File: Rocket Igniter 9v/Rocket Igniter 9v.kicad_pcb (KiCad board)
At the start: 2 copper layers, 79.9 x 59.8 mm, 29 parts, among them J1 1711725, J2 1711725, K1 G5Q-1 DC5, Q1 BC327, Q2 PN2222ABU, SW1 Y201132C203NQ, SW2 M2011S3S1W01, SW3 RP3502ARED

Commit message: tidied the pcb
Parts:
- D2: value 1.5KExxCA -> P6KE6.8CA; footprint Diode_THT:D_DO-201AE_P15.24mm_Horizontal -> Diode_THT:D_DO-15_P10.16mm_Horizontal
- moved R5 11.3 mm to (186.3, 65.6)
- moved SW1 5.90 mm to (195.1, 70.5), turned to 180 degrees
- moved SW3 5.38 mm to (187.0, 59.7), turned to 90 degrees
- moved LED3 4.10 mm to (179.9, 72.7)
- moved J2 1.33 mm to (221.0, 78.9)
- moved D2 1.11 mm to (170.4, 66.4)
- moved J1 0.48 mm to (157.0, 84.0)
- renumbered REF** to locked
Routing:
- net -BATT: track 14.8 -> 207.3 mm
- net Net-(D2-Pad1): track 36.9 -> 29.3 mm
- net Net-(LED3-Pad2): track 13.5 -> 6.13 mm
- net +5V: track 71.2 -> 77.2 mm
- net Net-(R5-Pad1): track 11.4 -> 6.45 mm
- net Net-(D2-Pad2): track 54.3 -> 51.8 mm
- removed copper zone on B.Cu, net -BATT
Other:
- net class Default removed

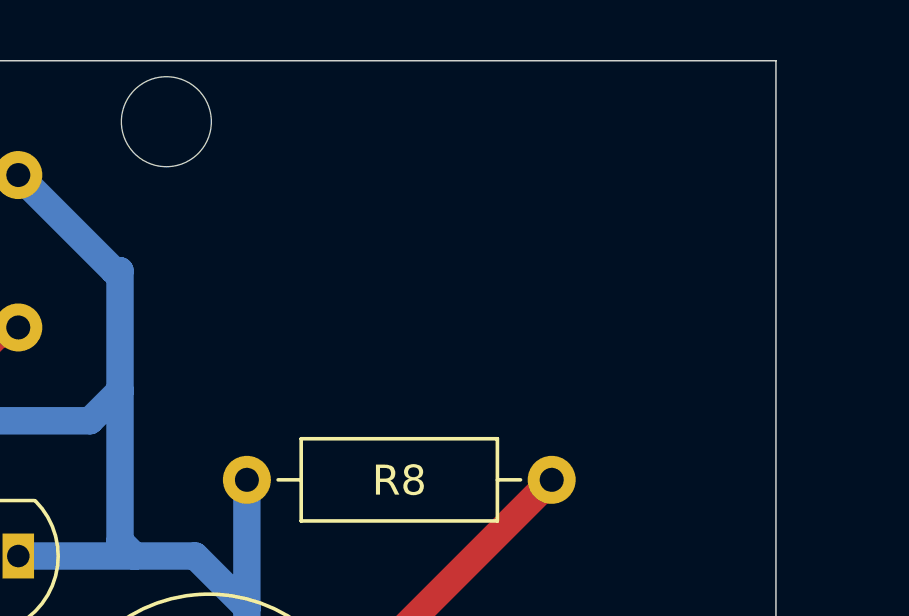
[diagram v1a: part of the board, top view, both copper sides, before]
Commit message: adjust silkscreen
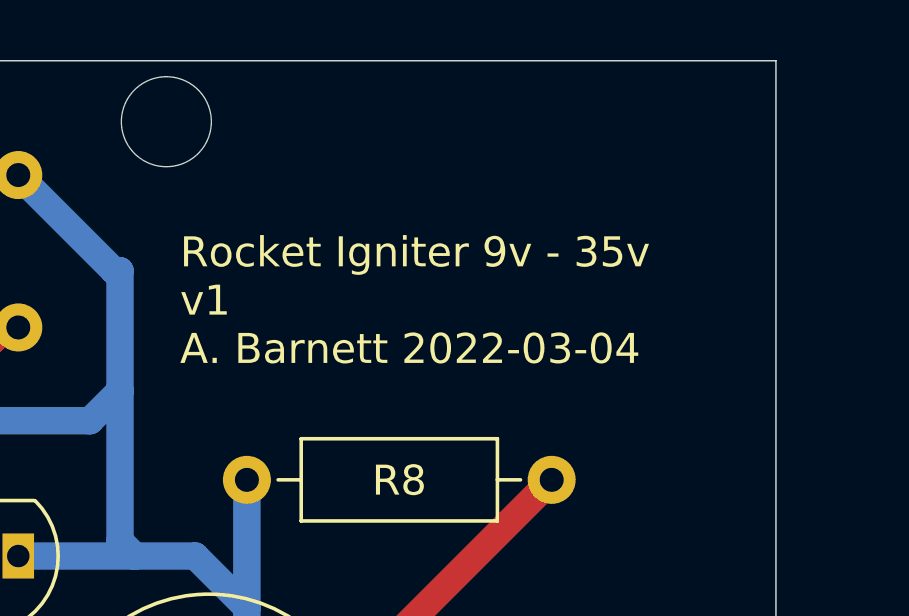
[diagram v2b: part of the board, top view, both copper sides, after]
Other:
- rule pad_to_mask_clearance: 0.051 -> 0
- board text added: "Rocket Igniter 9v - 35v v1 A. Barnett 2022-03-04"
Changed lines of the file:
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@@
   )
   (setup
-    (pad_to_mask_clearance 0.051)
-    (solder_mask_min_width 0.25)
+    (stackup
+      (layer "F.SilkS" (type "Top Silk Screen"))
+      (layer "F.Paste" (type "Top Solder Paste"))
+      (layer "F.Mask" (type "Top Solder Mask") (thickness 0.01))
+      (layer "F.Cu" (type "copper") (thickness 0.035))
+      (layer "dielectric 1" (type "core") (thickness 1.51) (material "FR4") (epsilon_r 4.5) (loss_tangent 0.02))
+      (layer "B.Cu" (type "copper") (thickness 0.035))
+      (layer "B.Mask" (type "Bottom Solder Mask") (thickness 0.01))
+      (layer "B.Paste" (type "Bottom Solder Paste"))
+      (layer "B.SilkS" (type "Bottom Silk Screen"))
+      (copper_finish "None")
+      (dielectric_constraints no)
+    )
+    (pad_to_mask_clearance 0)
     (grid_origin 148.58746 50.90414)
     (pcbplotparams
@@
       (disableapertmacros false)
       (usegerberextensions false)
-      (usegerberattributes false)
-      (usegerberadvancedattributes false)
+      (usegerberattributes true)
+      (usegerberadvancedattributes true)
       (creategerberjobfile false)
       (svguseinch false)
       (svgprecision 6)
-      (excludeedgelayer true)
+      (excludeedgelayer false)
       (plotframeref false)
       (viasonmask false)
       (mode 1)
-      (useauxorigin false)
+      (useauxorigin true)
       (hpglpennumber 1)
       (hpglpenspeed 20)
@@
       (outputformat 1)
       (mirror false)
-      (drillshape 1)
+      (drillshape 0)
       (scaleselection 1)
       (outputdirectory "")
@@
     (effects (font (size 1 1) (thickness 0.15)))
   )
+  (gr_text "Rocket Igniter 9v - 35v\nv1\nA. Barnett 2022-03-04" (at 208.58746 58.90414) (layer "F.SilkS")
+    (effects (font (size 1 1) (thickness 0.25)) (justify left))
+  )
   (segment (start 182.58746 62.90414) (end 181.58746 63.90414) (width 0.9144) (layer "B.Cu") (net 1))
